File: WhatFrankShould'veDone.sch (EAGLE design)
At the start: 52 parts, among them IC1 TLE5205-2G, IC2 TLE5205-2G, IC3 TLE5205-2G, IC5 TLE5205-2G, J3 POWERPOLE_DOUBLE, M0 Motor3, M1 Motor3, M2 Motor3, M3 Motor3, U1 LM2576.SMD

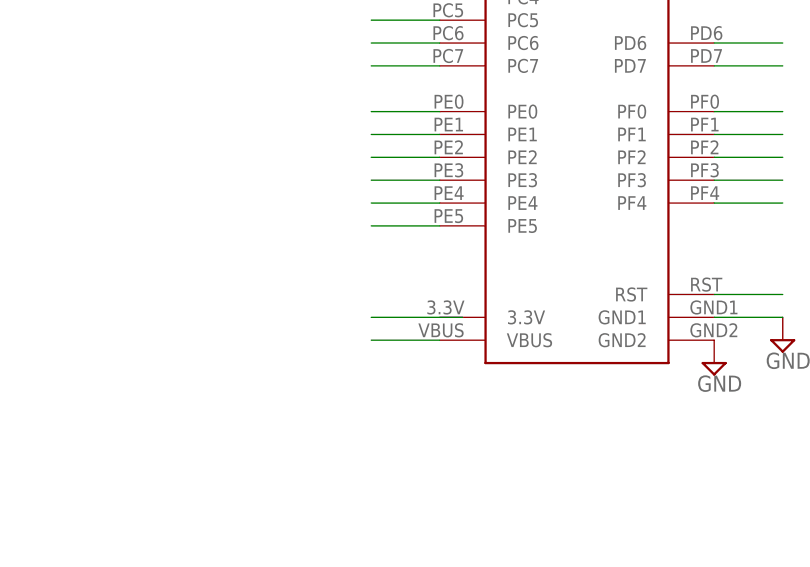
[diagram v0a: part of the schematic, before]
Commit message: Cleaned up airwires Added second ground plane Things missing:  Silkscreen comments  Mounting holes  Dounbhe check motor controller IC's pad connections
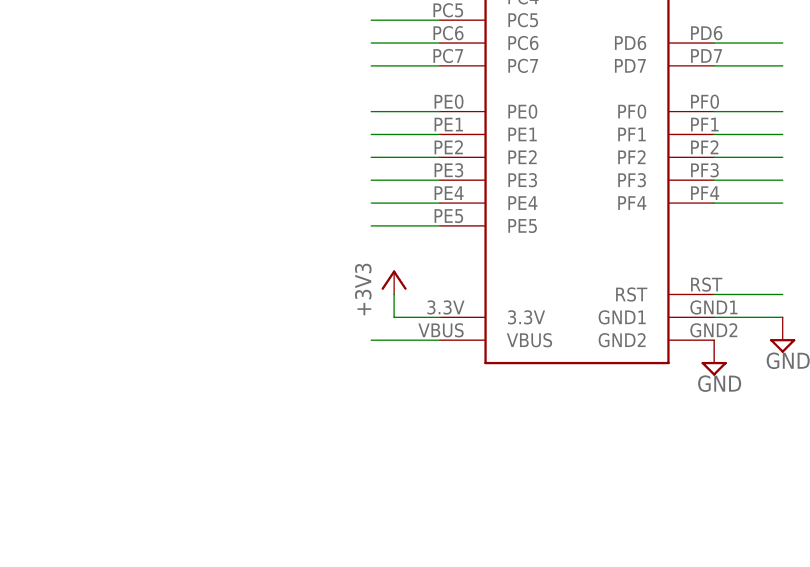
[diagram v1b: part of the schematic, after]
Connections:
- net +3V3: now also U$1.3.3V
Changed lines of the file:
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@@
 <?xml version="1.0" encoding="utf-8"?>
 <!DOCTYPE eagle SYSTEM "eagle.dtd">
-<eagle version="6.3">
+<eagle version="6.4">
 <drawing>
 <settings>
@@
 <grid distance="0.1" unitdist="inch" unit="inch" style="lines" multiple="1" display="no" altdistance="0.01" altunitdist="inch" altunit="inch"/>
 <layers>
-<layer number="1" name="Top" color="4" fill="1" visible="yes" active="no"/>
-<layer number="16" name="Bottom" color="1" fill="1" visible="yes" active="no"/>
-<layer number="17" name="Pads" color="2" fill="1" visible="yes" active="no"/>
-<layer number="18" name="Vias" color="2" fill="1" visible="yes" active="no"/>
-<layer number="19" name="Unrouted" color="6" fill="1" visible="yes" active="no"/>
-<layer number="20" name="Dimension" color="15" fill="1" visible="yes" active="no"/>
-<layer number="21" name="tPlace" color="7" fill="1" visible="yes" active="no"/>
-<layer number="22" name="bPlace" color="7" fill="1" visible="yes" active="no"/>
-<layer number="23" name="tOrigins" color="15" fill="1" visible="yes" active="no"/>
-<layer number="24" name="bOrigins" color="15" fill="1" visible="yes" active="no"/>
-<layer number="25" name="tNames" color="7" fill="1" visible="yes" active="no"/>
-<layer number="26" name="bNames" color="7" fill="1" visible="yes" active="no"/>
-<layer number="27" name="tValues" color="7" fill="1" visible="yes" active="no"/>
-<layer number="28" name="bValues" color="7" fill="1" visible="yes" active="no"/>
+<layer number="1" name="Top" color="4" fill="1" visible="no" active="no"/>
+<layer number="16" name="Bottom" color="1" fill="1" visible="no" active="no"/>
+<layer number="17" name="Pads" color="2" fill="1" visible="no" active="no"/>
+<layer number="18" name="Vias" color="2" fill="1" visible="no" active="no"/>
+<layer number="19" name="Unrouted" color="6" fill="1" visible="no" active="no"/>
+<layer number="20" name="Dimension" color="15" fill="1" visible="no" active="no"/>
+<layer number="21" name="tPlace" color="7" fill="1" visible="no" active="no"/>
+<layer number="22" name="bPlace" color="7" fill="1" visible="no" active="no"/>
+<layer number="23" name="tOrigins" color="15" fill="1" visible="no" active="no"/>
+<layer number="24" name="bOrigins" color="15" fill="1" visible="no" active="no"/>
+<layer number="25" name="tNames" color="7" fill="1" visible="no" active="no"/>
+<layer number="26" name="bNames" color="7" fill="1" visible="no" active="no"/>
+<layer number="27" name="tValues" color="7" fill="1" visible="no" active="no"/>
+<layer number="28" name="bValues" color="7" fill="1" visible="no" active="no"/>
 <layer number="29" name="tStop" color="7" fill="3" visible="no" active="no"/>
 <layer number="30" name="bStop" color="7" fill="6" visible="no" active="no"/>
@@
 <layer number="35" name="tGlue" color="7" fill="4" visible="no" active="no"/>
 <layer number="36" name="bGlue" color="7" fill="5" visible="no" active="no"/>
-<layer number="37" name="tTest" color="7" fill="1" visible="yes" active="no"/>
-<layer number="38" name="bTest" color="7" fill="1" visible="yes" active="no"/>
+<layer number="37" name="tTest" color="7" fill="1" visible="no" active="no"/>
+<layer number="38" name="bTest" color="7" fill="1" visible="no" active="no"/>
 <layer number="39" name="tKeepout" color="4" fill="11" visible="no" active="no"/>
 <layer number="40" name="bKeepout" color="1" fill="11" visible="no" active="no"/>
@@
 <layer number="44" name="Drills" color="7" fill="1" visible="no" active="no"/>
 <layer number="45" name="Holes" color="7" fill="1" visible="no" active="no"/>
-<layer number="46" name="Milling" color="3" fill="1" visible="yes" active="no"/>
-<layer number="47" name="Measures" color="7" fill="1" visible="yes" active="no"/>
-<layer number="48" name="Document" color="7" fill="1" visible="yes" active="no"/>
-<layer number="49" name="Reference" color="7" fill="1" visible="yes" active="no"/>
-<layer number="50" name="dxf" color="7" fill="1" visible="yes" active="no"/>
-<layer number="51" name="tDocu" color="7" fill="1" visible="yes" active="no"/>
-<layer number="52" name="bDocu" color="7" fill="1" visible="yes" active="no"/>
-<layer number="53" name="tGND_GNDA" color="7" fill="9" visible="yes" active="no"/>
-<layer number="54" name="bGND_GNDA" color="1" fill="9" visible="yes" active="no"/>
-<layer number="56" name="wert" color="7" fill="1" visible="yes" active="no"/>
-<layer number="59" name="tCarbon" color="7" fill="1" visible="yes" active="no"/>
-<layer number="60" name="bCarbon" color="7" fill="1" visible="yes" active="no"/>
+<layer number="46" name="Milling" color="3" fill="1" visible="no" active="no"/>
+<layer number="47" name="Measures" color="7" fill="1" visible="no" active="no"/>
+<layer number="48" name="Document" color="7" fill="1" visible="no" active="no"/>
+<layer number="49" name="Reference" color="7" fill="1" visible="no" active="no"/>
+<layer number="50" name="dxf" color="7" fill="1" visible="no" active="no"/>
+<layer number="51" name="tDocu" color="7" fill="1" visible="no" active="no"/>
+<layer number="52" name="bDocu" color="7" fill="1" visible="no" active="no"/>
+<layer number="53" name="tGND_GNDA" color="7" fill="9" visible="no" active="no"/>
+<layer number="54" name="bGND_GNDA" color="1" fill="9" visible="no" active="no"/>
+<layer number="56" name="wert" color="7" fill="1" visible="no" active="no"/>
+<layer number="59" name="tCarbon" color="7" fill="1" visible="no" active="no"/>
+<layer number="60" name="bCarbon" color="7" fill="1" visible="no" active="no"/>
 <layer number="91" name="Nets" color="2" fill="1" visible="yes" active="yes"/>
 <layer number="92" name="Busses" color="1" fill="1" visible="yes" active="yes"/>
@@
 <part name="C11" library="microbuilder" deviceset="CAP_ELECTROLYTIC" device="PANASONIC_D" value="100uF"/>
 <part name="C12" library="microbuilder" deviceset="CAP_ELECTROLYTIC" device="PANASONIC_D" value="1000uF"/>
+<part name="+3V6" library="supply1" deviceset="+3V3" device=""/>
 </parts>
 <sheets>
@@
 <instance part="C11" gate="G$1" x="104.14" y="-25.4"/>
 <instance part="C12" gate="G$1" x="167.64" y="-30.48"/>
+<instance part="+3V6" gate="G$1" x="121.92" y="40.64"/>
 </instances>
 <busses>
@@
 <wire x1="194.31" y1="101.6" x2="194.31" y2="107.95" width="0.1524" layer="91"/>
 </segment>
+<segment>
+<pinref part="+3V6" gate="G$1" pin="+3V3"/>
+<wire x1="121.92" y1="35.56" x2="121.92" y2="38.1" width="0.1524" layer="91"/>
+<pinref part="U$1" gate="G$1" pin="3.3V"/>
+<wire x1="121.92" y1="35.56" x2="127" y2="35.56" width="0.1524" layer="91"/>
+</segment>
 </net>
 <net name="N$7" class="0">
@@
 </segment>
 </net>
-<net name="3.3V" class="0">
-<segment>
-<wire x1="129.54" y1="35.56" x2="119.38" y2="35.56" width="0.1524" layer="91"/>
-</segment>
-</net>

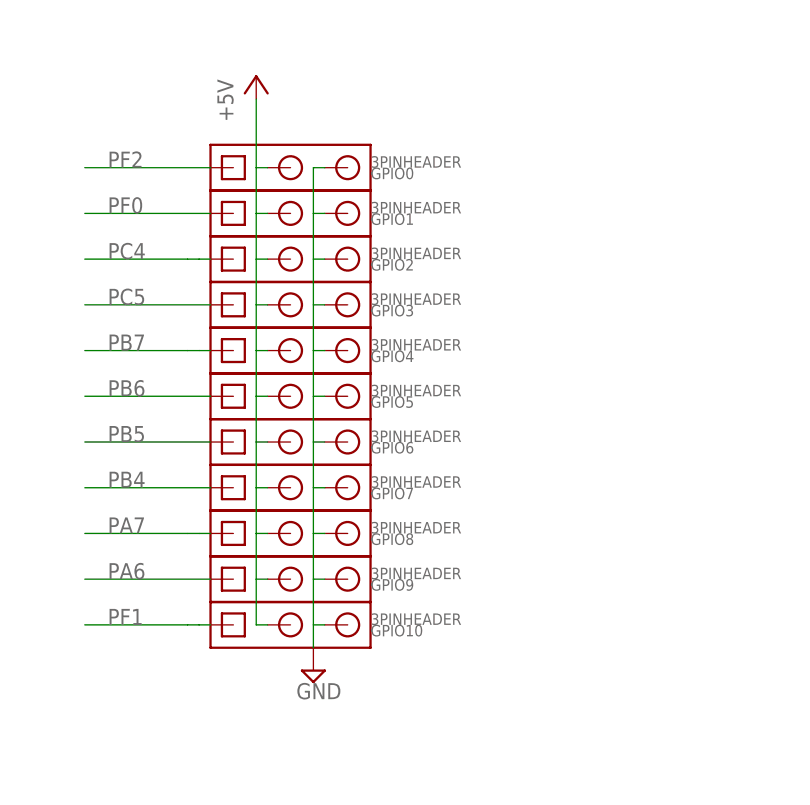
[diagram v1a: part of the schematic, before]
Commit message: Changed traces slightly
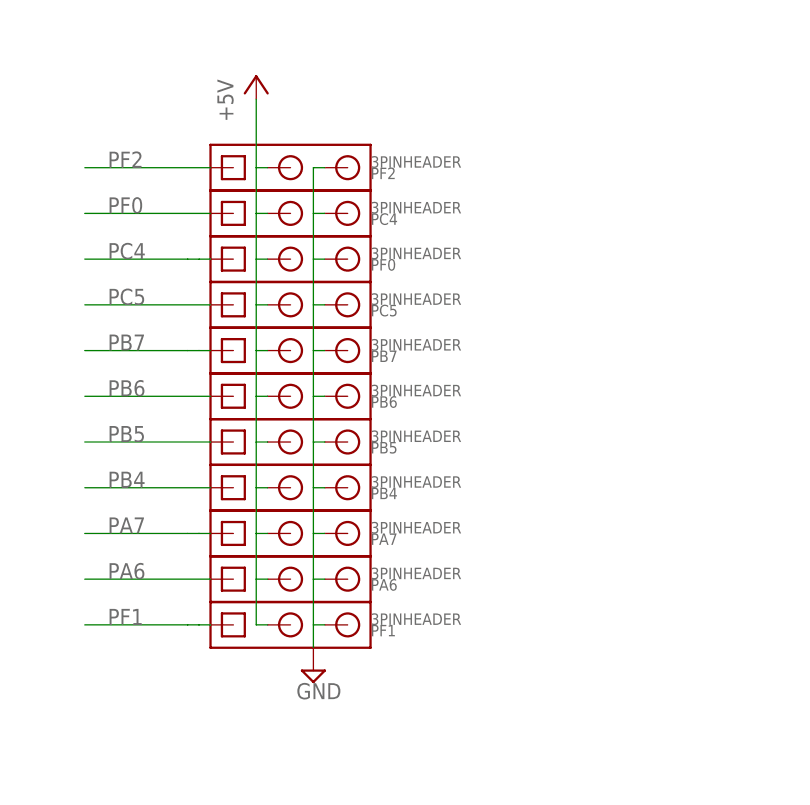
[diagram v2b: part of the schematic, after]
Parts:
- renumbered GPIO0 to PF2, GPIO1 to PC4, GPIO10 to PF1, GPIO2 to PF0, GPIO3 to PC5, GPIO4 to PB7, GPIO5 to PB6, GPIO6 to PB5, GPIO7 to PB4, GPIO8 to PA7, GPIO9 to PA6
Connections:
- net GND renamed -GND
